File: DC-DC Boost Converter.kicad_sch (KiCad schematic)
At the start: 13 parts, among them J1 Conn_01x01_Pin, J2 Conn_01x01_Pin, J3 Conn_01x01_Pin, J4 Conn_01x01_Pin

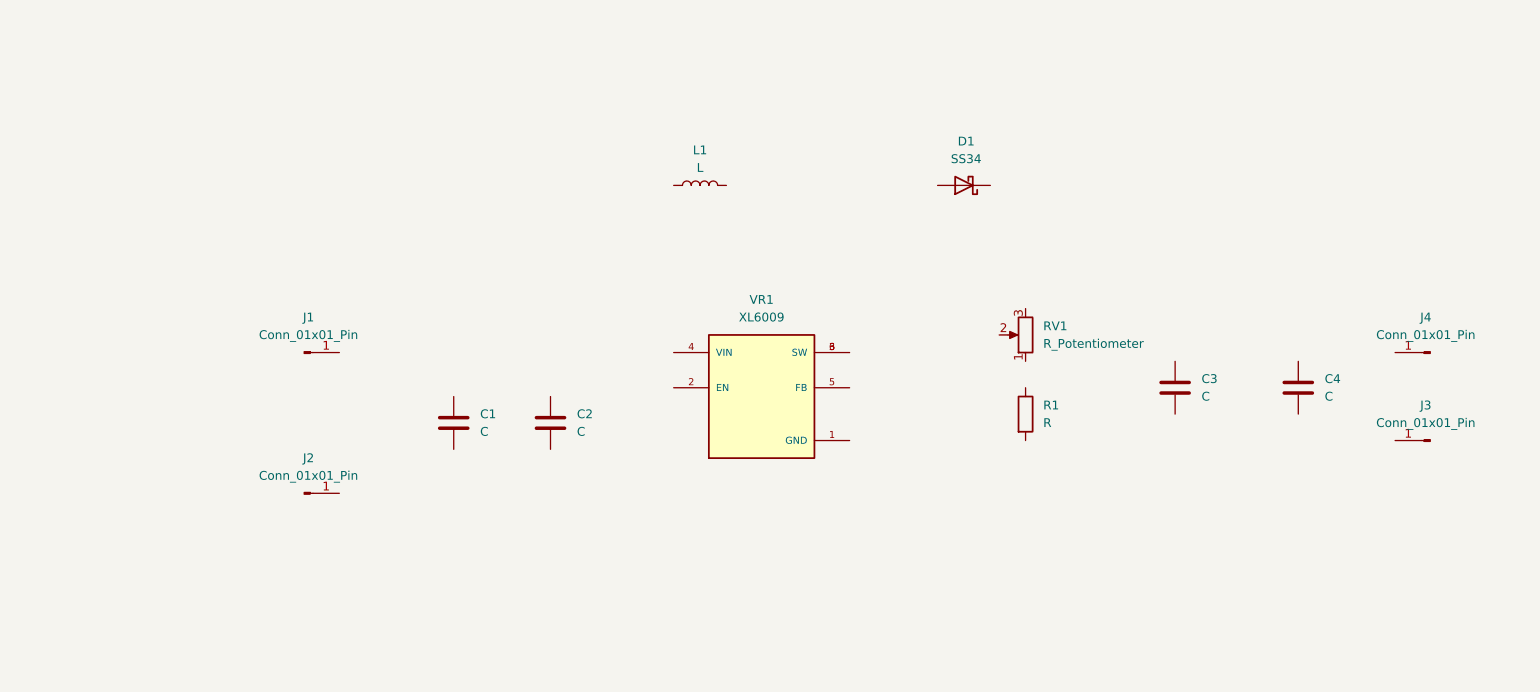
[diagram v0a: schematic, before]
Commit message: Added Wires to Components
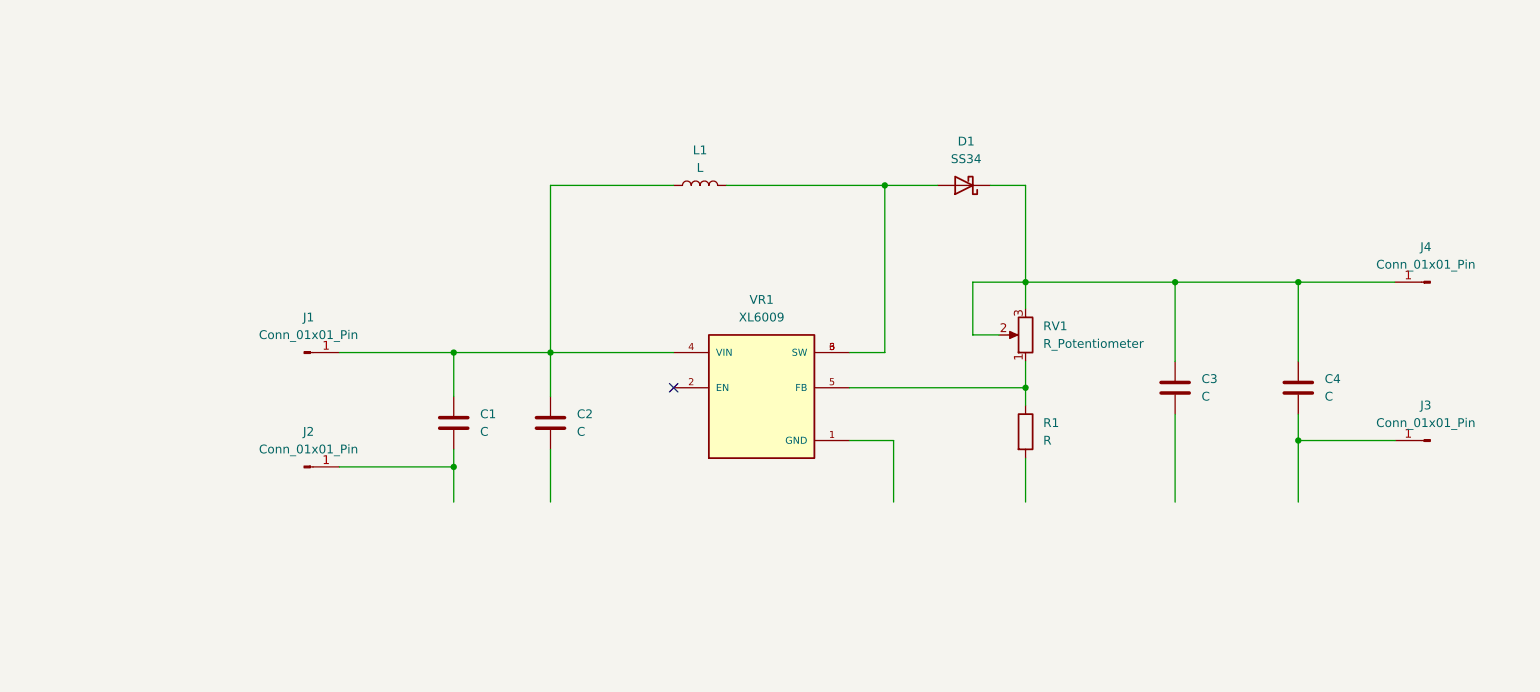
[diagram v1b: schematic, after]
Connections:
- net at J4.1 (Pin_1): now also C3.1, C4.1, D1.1 (K), RV1.2, RV1.3
- net at R1.1: now also RV1.1, VR1.5 (FB)
- net at VR1.3 (SW), VR1.6 (SW): now also D1.2 (A), L1.2
- net at VR1.4 (VIN): now also C1.1, C2.1, J1.1 (Pin_1), L1.1
- net at C4.2: now also J3.1 (Pin_1)
- net at C1.2: now also J2.1 (Pin_1)
- no-connect marks 0 -> 1
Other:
- moved on the sheet: J2, J4, R1

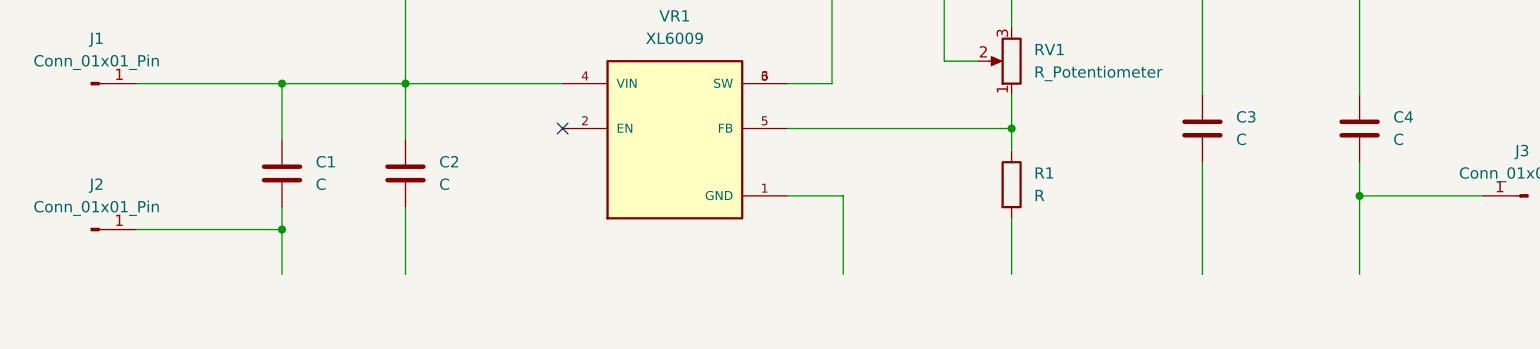
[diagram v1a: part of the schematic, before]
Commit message: Added GND and PWR flag
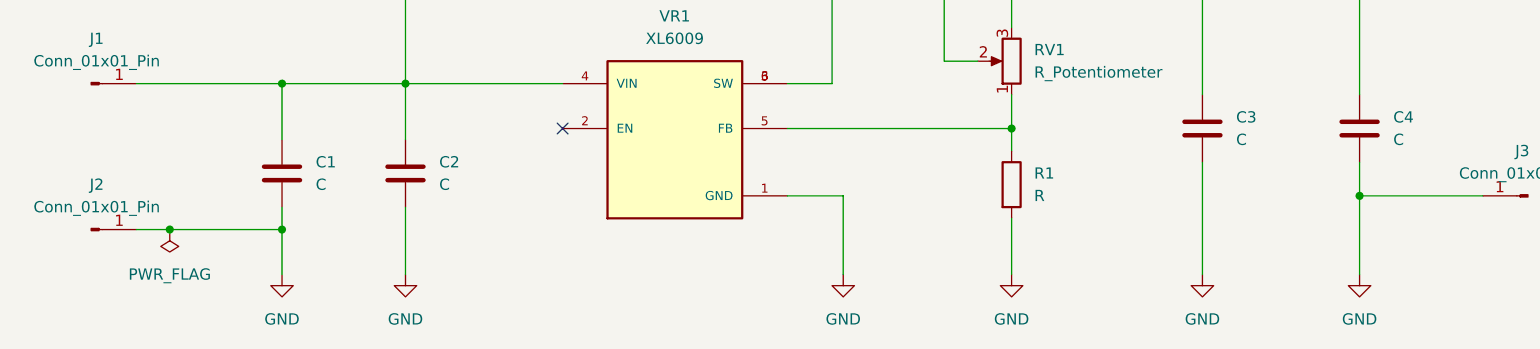
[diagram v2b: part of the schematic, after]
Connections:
- net GND: now reaches R1.2
- net GND: now also C1.2, C2.2, C3.2, C4.2, J2.1 (Pin_1), J3.1 (Pin_1), VR1.1 (GND)

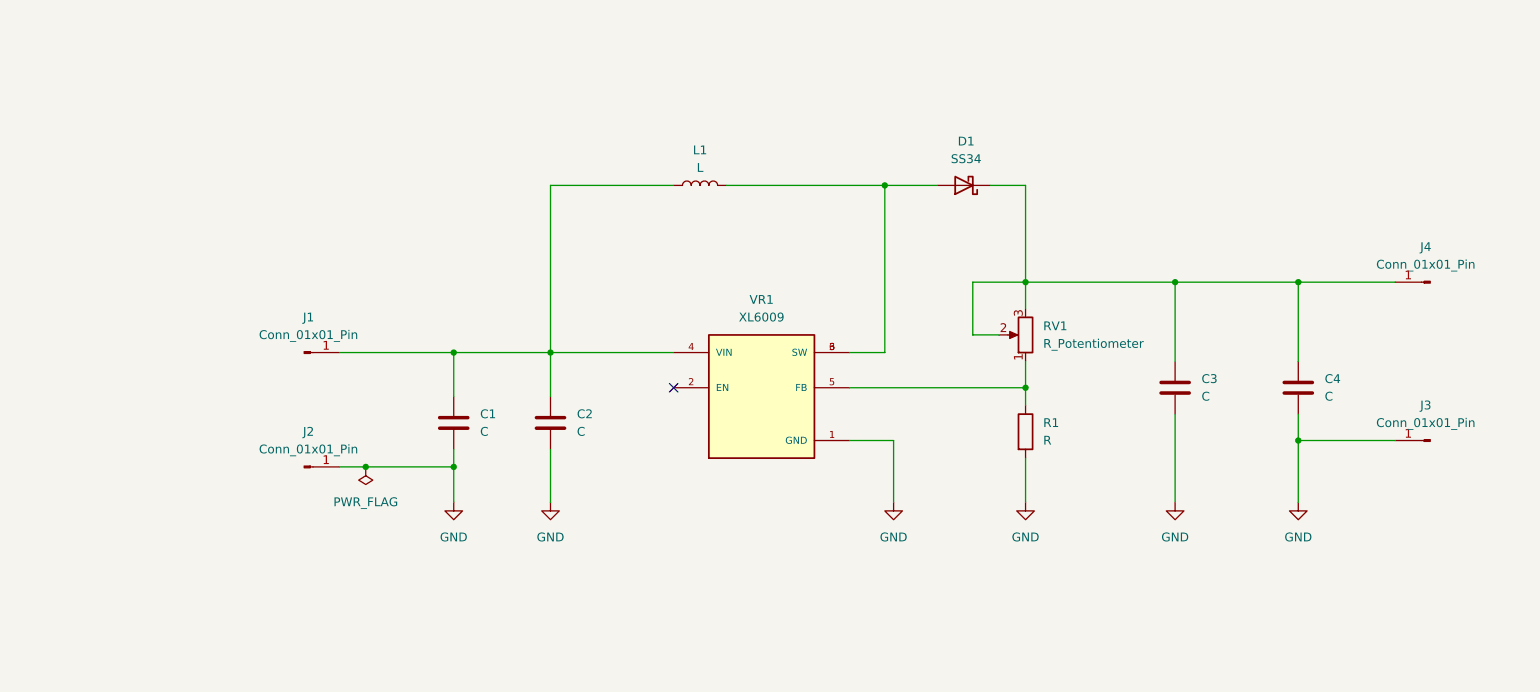
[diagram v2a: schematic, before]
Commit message: Added Values to Components
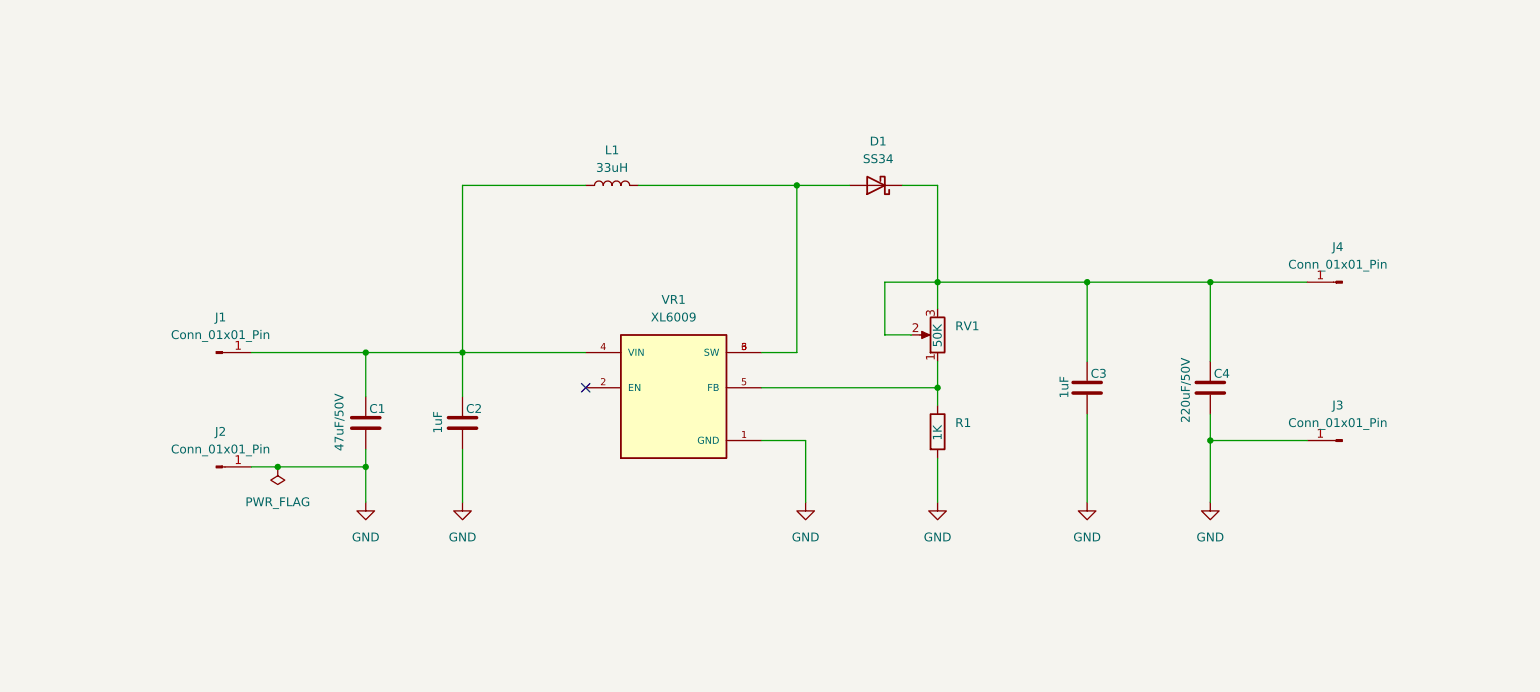
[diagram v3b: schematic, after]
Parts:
- C1: value C -> 47uF/50V
- C2, C3: value C -> 1uF
- C4: value C -> 220uF/50V
- L1: value L -> 33uH
- R1: value R -> 1K
- RV1: value R_Potentiometer -> 50K
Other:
- moved on the sheet: C1, C2, C3, C4, D1, J1, J2, J3, J4, L1, R1, RV1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

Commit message: Shematic in Schematic editor
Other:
- note added: "VIN"
- note added: "VOUT"
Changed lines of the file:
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@@
 		(title "DC-DC Boost Converter")
+	)
+	(text "VIN"
+		(exclude_from_sim no)
+		(at 51.816 100.33 0)
+		(effects
+			(font
+				(size 6.35 6.35)
+			)
+		)
+	)
+	(text "VOUT"
+		(exclude_from_sim no)
+		(at 239.268 91.948 0)
+		(effects
+			(font
+				(size 6.35 6.35)
+			)
+		)
 	)
 	(junction
@@
 		)
 	)
+	(polyline
+		(pts
+			(xy 38.1 135.89) (xy 38.1 43.815)
+		)
+		(stroke
+			(width 0)
+			(type dash)
+		)
+	)
 	(wire
 		(pts
@@
 		)
 	)
+	(polyline
+		(pts
+			(xy 253.365 43.815) (xy 253.365 135.255)
+		)
+		(stroke
+			(width 0)
+			(type dash)
+		)
+	)
 	(wire
 		(pts
@@
 		)
 	)
+	(polyline
+		(pts
+			(xy 38.1 43.815) (xy 253.365 43.815)
+		)
+		(stroke
+			(width 0)
+			(type dash)
+		)
+	)

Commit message: Final Schematic
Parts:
- C1, C4: footprint (none) -> Capacitor_THT:C_Radial_D6.3mm_H11.0mm_P2.50mm
- C2, C3: footprint (none) -> Capacitor_SMD:C_0805_2012Metric
- J1, J2, J3, J4: footprint (none) -> Connector_PinHeader_2.54mm:PinHeader_1x01_P2.54mm_Vertical
- L1: footprint (none) -> Inductor_SMD:L_12x12mm_H8mm
- R1: footprint (none) -> Resistor_SMD:R_1206_3216Metric
- RV1: footprint (none) -> Potentiometer_THT:Potentiometer_Bourns_3296W_Vertical
- VR1: footprint XL6009:DPAK170P1435X465-6N -> Footprints:DPAK170P1435X465-6N
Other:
- moved on the sheet: C1, C2, C3, C4, D1, J1, J2, J3, J4, L1, R1, RV1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
